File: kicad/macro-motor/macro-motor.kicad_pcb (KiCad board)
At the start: 2 copper layers, 104 parts, among them J101 CAN+PWR, J102 3V3, J103 5V, J104 GND, J105 Gpio, J106 U, J107 V, J108 W, J109 Conn_01x03_Female, J201 GND, J202 B, J203 A, J301 A, J302 B, J303 C, J501 SCL, J502 SDA, J503 3V3, J504 GND, J601 SWD, J604 TX, J605 OP_INM, J606 OP_OUT, J607 PA0, J608 PH1, J609 PH0, Q301 FDMD82xx, Q302 FDMD82xx, Q303 FDMD82xx, U101 ADP7112ACBZ-3.3-R7, U102 ADP7112ACBZ-5.0-R7, U201 AS5045B, U301 DRV8323S, U401 TCAN330, U501 TMP006, U601 STM32L433C(B-C)Ux_u

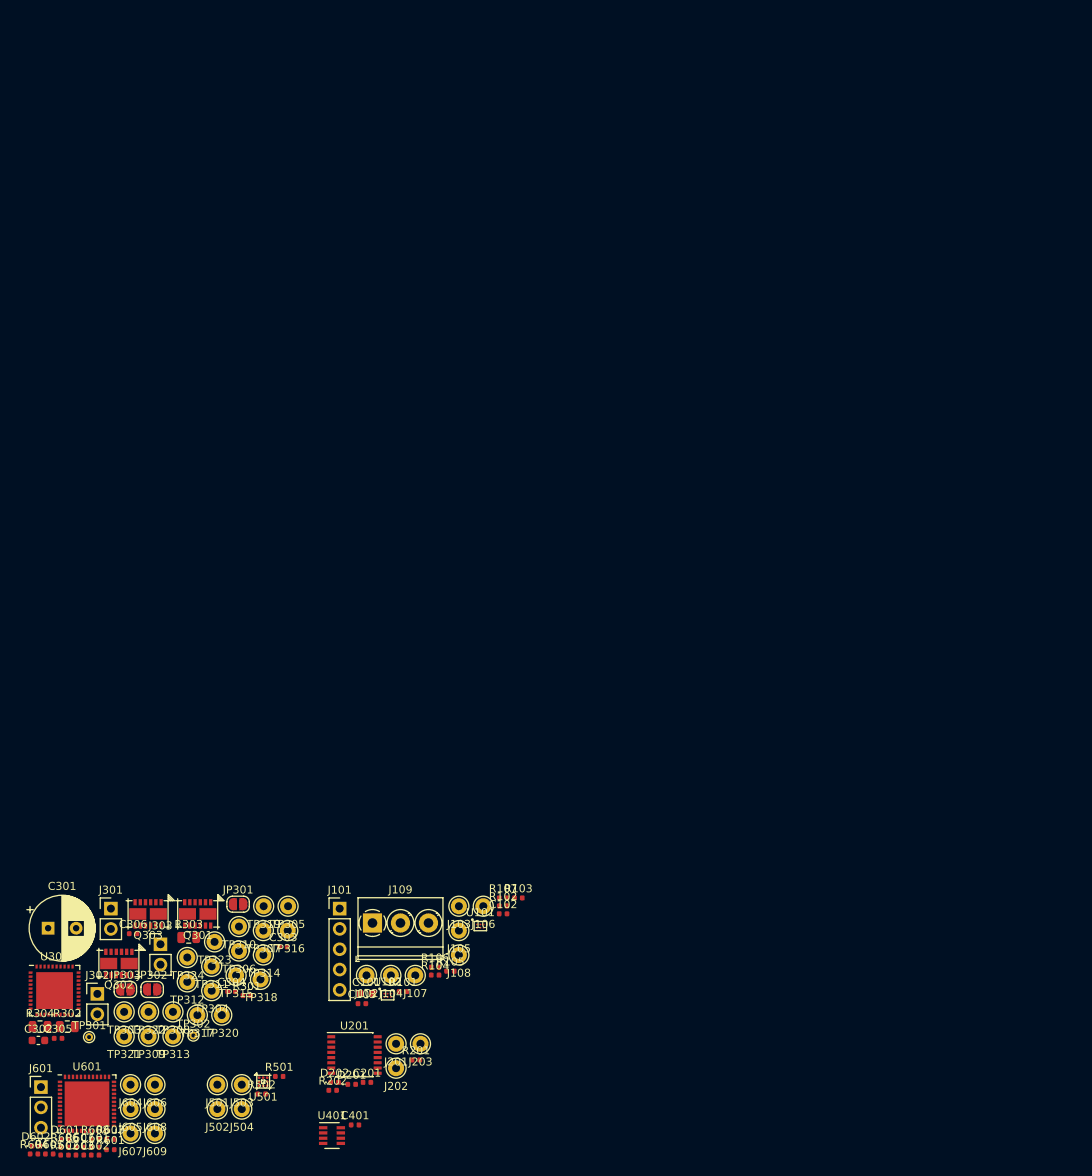
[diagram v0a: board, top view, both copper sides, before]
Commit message: macro-motor: PCB Layout
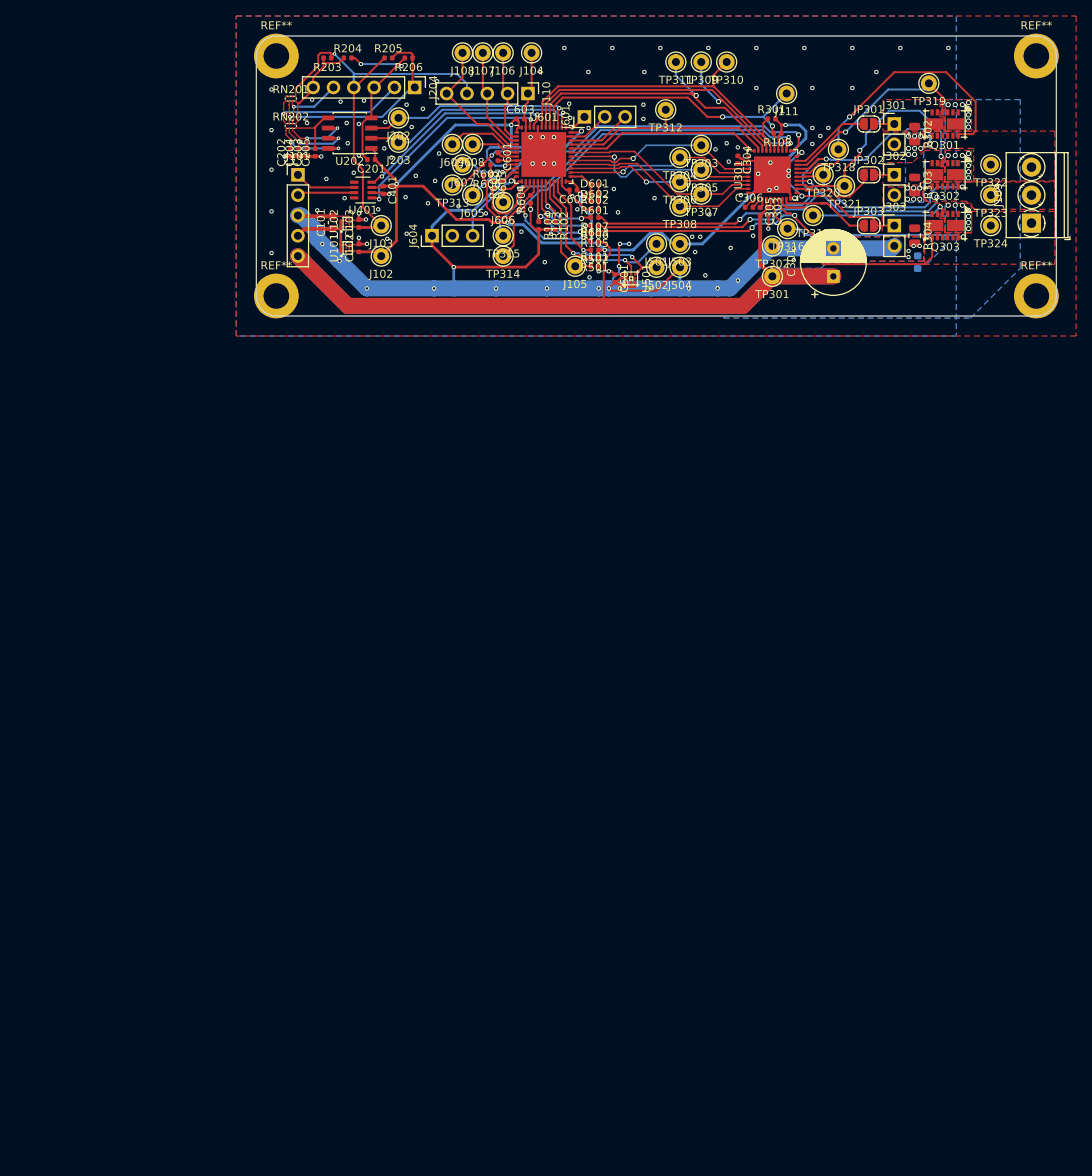
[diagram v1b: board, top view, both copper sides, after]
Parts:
- removed D201: Red, LED_SMD:LED_0402_1005Metric
- removed D202: Yellow, LED_SMD:LED_0402_1005Metric
- removed J201: GND, Connector_Pin:Pin_D1.0mm_L10.0mm
- removed R201, R202: 1k, Resistor_SMD:R_0402_1005Metric
- removed U201: AS5045B, Package_SO:SSOP-16_4.4x5.2mm_P0.65mm
- added C202: (2n7), Capacitor_SMD:C_0402_1005Metric, F.Cu at (106.8, 67.1)
- added C203: (2n7), Capacitor_SMD:C_0402_1005Metric, F.Cu at (108.8, 67.1)
- added C204: (2n7), Capacitor_SMD:C_0402_1005Metric, F.Cu at (107.8, 67.1)
- added C205: (2n7), Capacitor_SMD:C_0402_1005Metric, F.Cu at (109.9, 67.1)
- added C501: 100n, Capacitor_SMD:C_0402_1005Metric, F.Cu at (147.3, 82.8)
- added J110: HALL, Connector_PinHeader_2.54mm:PinHeader_1x05_P2.54mm_Vertical, F.Cu at (136.4, 59.7)
- added J111: Fault, Connector_Pin:Pin_D1.0mm_L10.0mm, F.Cu at (168.8, 59.7)
- added J204: Encoder, Connector_PinHeader_2.54mm:PinHeader_1x06_P2.54mm_Vertical, F.Cu at (122.3, 58.9)
- added R108: (10k), Resistor_SMD:R_0402_1005Metric, F.Cu at (167.6, 64.6)
- added R203: 47k, Resistor_SMD:R_0402_1005Metric, F.Cu at (111.4, 55.2)
- added R204: 47k, Resistor_SMD:R_0402_1005Metric, F.Cu at (113.9, 55.2)
- added R205: 47k, Resistor_SMD:R_0402_1005Metric, F.Cu at (119.0, 55.2)
- added R206: 47k, Resistor_SMD:R_0402_1005Metric, F.Cu at (121.5, 55.2)
- added REF**: MountingHole_3.2mm_M3_DIN965_Pad, MountingHole:MountingHole_3.2mm_M3_DIN965_Pad, F.Cu at (105.0, 55.0)
- added REF**: MountingHole_3.2mm_M3_DIN965_Pad, MountingHole:MountingHole_3.2mm_M3_DIN965_Pad, F.Cu at (105.0, 85.0)
- added REF**: MountingHole_3.2mm_M3_DIN965_Pad, MountingHole:MountingHole_3.2mm_M3_DIN965_Pad, F.Cu at (200.0, 85.0)
- added REF**: MountingHole_3.2mm_M3_DIN965_Pad, MountingHole:MountingHole_3.2mm_M3_DIN965_Pad, F.Cu at (200.0, 55.0)
- added RN201: (2k7), local-lib:EXB18V, F.Cu at (106.8, 60.3)
- added RN202: (100), local-lib:EXB18V, F.Cu at (106.8, 63.7)
- added U202: UA9637, Package_SO:SOIC-8_3.9x4.9mm_P1.27mm, F.Cu at (114.2, 64.6)
- C101: value 2µ2 16V -> 4µ7 16V
- C302: moved to B.Cu
- C601: value 10n??? -> 100n
- J604: value TX -> UART; footprint Connector_Pin:Pin_D1.0mm_L10.0mm -> Connector_PinHeader_2.54mm:PinHeader_1x03_P2.54mm_Vertical
- TP301, TP302: footprint TestPoint:TestPoint_THTPad_D1.0mm_Drill0.5mm -> Connector_Pin:Pin_D1.0mm_L10.0mm
- moved R302 153.8 mm to (184.8, 64.8), turned to 270 degrees
- moved TP322 149.3 mm to (194.3, 68.6)
- moved R304 147.4 mm to (184.8, 77.5), turned to 270 degrees
- moved C302 146.8 mm to (185.2, 80.8), turned to 90 degrees
- moved J302 142.9 mm to (182.2, 69.8)
- moved Q302 142.8 mm to (188.6, 69.8)
- moved C603 140.7 mm to (135.5, 62.9)
- moved TP309 140.0 mm to (158.1, 55.8)
- moved TP321 139.3 mm to (176.0, 71.2)
- moved J601 139.0 mm to (143.5, 62.6), turned to 90 degrees
- moved D602 139.0 mm to (144.8, 71.1), turned to 180 degrees
- moved J301 138.6 mm to (182.2, 63.5)
- moved Q301 135.9 mm to (188.6, 63.5)
- moved TP324 135.9 mm to (194.3, 76.2)
- moved U301 135.8 mm to (167.0, 69.8), turned to 90 degrees
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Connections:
- net Net-(J607-Pad1) renamed /Microcontroller/PA0
- net Net-(J608-Pad1) renamed /Microcontroller/PH1
- net Net-(J609-Pad1) renamed /Microcontroller/PH0
- J202 pad 1: /Encoder/A -> /Encoder/B
- J203 pad 1: /Encoder/B -> /Encoder/A
- J604 pad 1: /Microcontroller/TX -> GND
- Q303 pad 14: Net-(Q303-Pad14) -> Net-(J301-Pad2)
- Q303 pad 5: Net-(Q303-Pad14) -> Net-(J301-Pad2)
- Q303 pad 6: Net-(Q303-Pad14) -> Net-(J301-Pad2)
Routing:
- net GND: track 0.00 -> 255.2 mm, vias 0 -> 129
- net +24V: track 0.00 -> 163.8 mm, vias 0 -> 23
- net +3V3: track 0.00 -> 155.2 mm, vias 0 -> 10
- net +5V: track 0.00 -> 61.6 mm, vias 0 -> 1
- net /Microcontroller/CurrentV: track 0.00 -> 58.9 mm, vias 0 -> 2
- net /Microcontroller/CurrentU: track 0.00 -> 55.9 mm, vias 0 -> 2
- net /Motor_Driver/OUT_W: track 0.00 -> 55.2 mm, vias 0 -> 3
- net /Motor_Driver/OUT_U: track 0.00 -> 53.2 mm, vias 0 -> 2
- net /Motor_Driver/OUT_V: track 0.00 -> 49.9 mm, vias 0 -> 3
- net /Microcontroller/CurrentW: track 0.00 -> 49.4 mm, vias 0 -> 2
- net /Microcontroller/MISO: track 0.00 -> 42.5 mm
- net /Microcontroller/MOSI: track 0.00 -> 41.4 mm, vias 0 -> 1
- net /Microcontroller/SCK: track 0.00 -> 39.3 mm, vias 0 -> 1
- net /Microcontroller/Fault: track 0.00 -> 39.2 mm, vias 0 -> 2
- net /Motor_Driver/GH_W: track 0.00 -> 37.6 mm, vias 0 -> 1
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- added copper zone on B.Cu, net +24V
- added copper zone on F.Cu, net +24V
- added copper zone on F.Cu, net /Motor_Driver/OUT_U
- added copper zone on F.Cu, net /Motor_Driver/OUT_V
- added copper zone on F.Cu, net /Motor_Driver/OUT_W
- added copper zone on B.Cu, net GND
- added copper zone on F.Cu, net GND
- added copper zone on F.Cu, net Net-(J301-Pad1)
- added copper zone on B.Cu, net Net-(J301-Pad2)
- added copper zone on F.Cu, net Net-(J301-Pad2)
- added copper zone on F.Cu, net Net-(J302-Pad1)
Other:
- board outline added: 100 x 35 mm
- rule trace_min: 0.2 -> 0.15
- rule via_min_drill: 0.3 -> 0.2
- rule via_min_size: 0.4 -> 0.45

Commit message: macro-motor: PCB Layout finished, silkscreen
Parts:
- added G***: LOGO, local-lib:aisler-logo, B.Cu at (137.8, 84.2)
- added G***: LOGO, local-lib:rca-logo, B.Cu at (144.0, 71.0)
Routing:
- net GND: vias 129 -> 132
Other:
- rule pad_to_mask_clearance: 0 -> 0.025
- board text added: "+24V"
- board text added: "+6V"
- board text added: "2× 2µ2 6V3"
- board text added: "2× ADP7112ACBZ (5V, 3V3)"
- board text added: "4x (2n7)"
- board text added: "CAN"
- board text added: "GND"
- board text added: "L H"
- board text added: "Sponsored by"
- board text added: "macro-motor"
- board text added: "rev1"
- board text added: "©Raphael Lehmann"

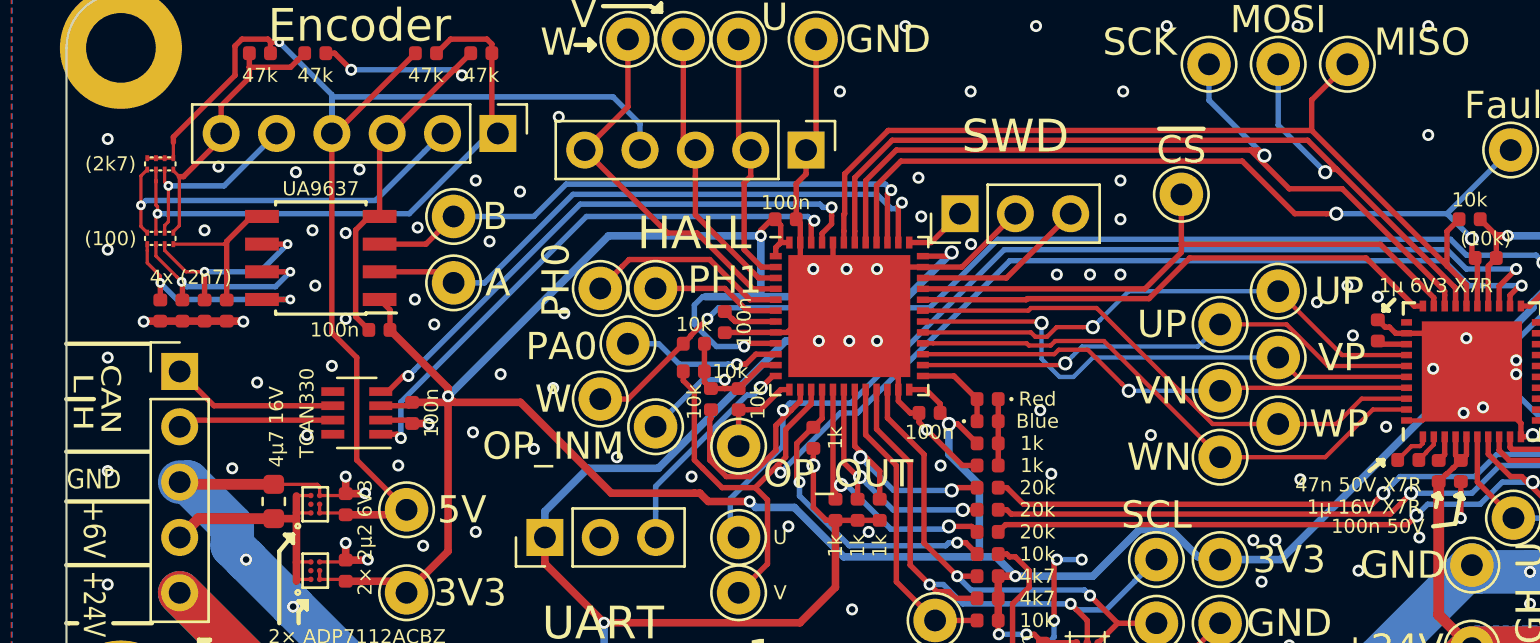
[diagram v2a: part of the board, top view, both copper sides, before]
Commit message: macro-motor: Minor fixes
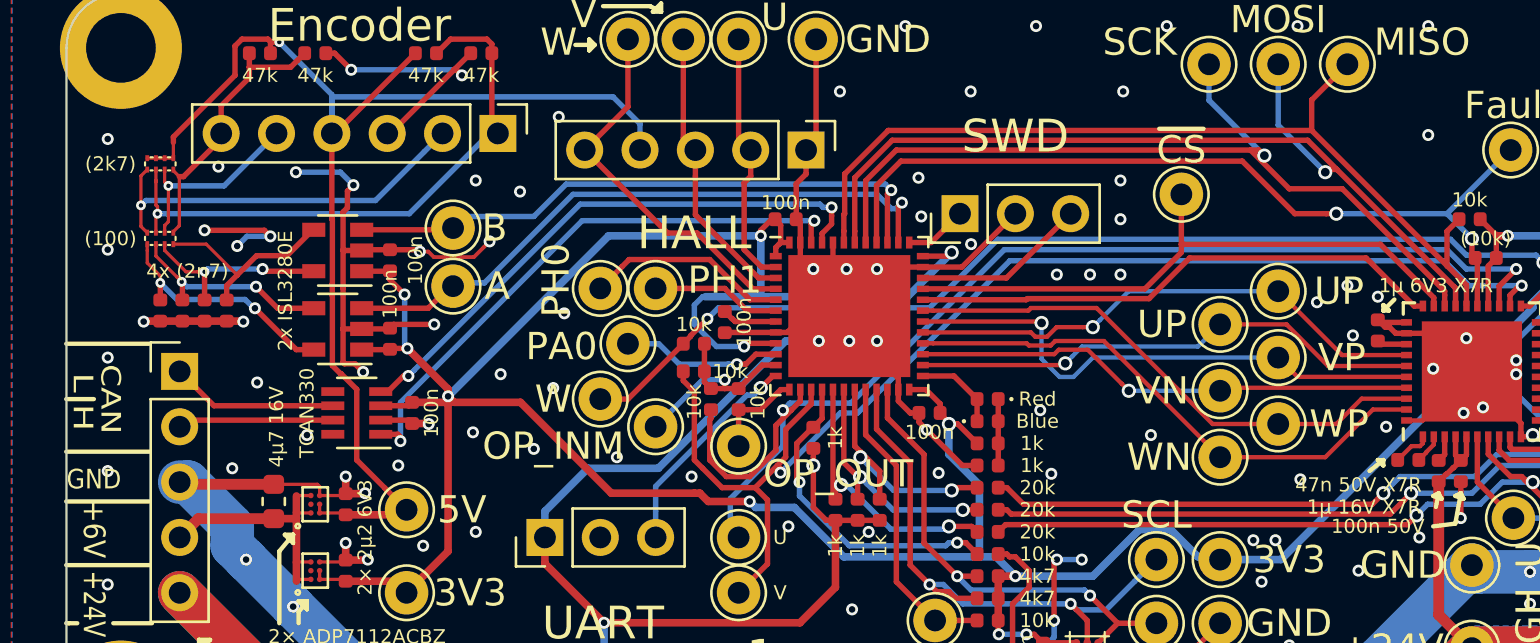
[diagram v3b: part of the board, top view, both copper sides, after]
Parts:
- added C206: 100n, Capacitor_SMD:C_0402_1005Metric, F.Cu at (117.3, 64.8)
- added U201: ISL3280E, Package_TO_SOT_SMD:SOT-23-5, F.Cu at (115.0, 64.3)
- U202: value UA9637 -> ISL3280E; footprint Package_SO:SOIC-8_3.9x4.9mm_P1.27mm -> Package_TO_SOT_SMD:SOT-23-5
- moved U202 3.35 mm to (115.0, 67.9)
- moved C201 0.63 mm to (117.3, 68.3), turned to 90 degrees
- moved J202 0.53 mm to (120.2, 63.3)
- moved J203 0.15 mm to (120.2, 65.9)
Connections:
- U202 pad 2: /Encoder/A -> GND
- U202 pad 3: /Encoder/B -> /Encoder/A
- U202 pad 4: GND -> Net-(C204-Pad2)
- U202 pad 5: Net-(C205-Pad2) -> Net-(C202-Pad2)
- U301 pad 31: (no net) -> GND
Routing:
- net GND: track 255.2 -> 275.5 mm, vias 132 -> 129
- net +3V3: track 155.2 -> 159.7 mm, vias 10 -> 12
- net Net-(C205-Pad2): track 7.28 -> 9.23 mm
- net /Encoder/A: track 28.1 -> 29.2 mm
- net Net-(C202-Pad2): track 10.4 -> 11.1 mm
- net /Encoder/B: track 27.2 -> 27.8 mm
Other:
- board text added: "2x ISL3280E"
